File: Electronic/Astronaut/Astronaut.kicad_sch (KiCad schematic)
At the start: 67 parts, among them J1 Conn_01x05, J2 Conn_01x04, J3 Conn_01x02, J4 Conn_01x02, J5 Conn_01x04, J6 Conn_01x04, J7 Conn_01x02, J8 Conn_01x10, SW1 SH-1808SN-250GF, SW2 SH-1808SN-250GF, U1 LAN8651B1-E/LMX, U2 AVRH10C221KT1R5YA8, U3 AVRH10C221KT1R5YA8, U4 MCP2518FDT-E/SL, U5 ATA6563-GAQW1, U6 ESD5451N_C5261080, U7 ESD5451N_C5261080, U8 ADS1115IDGSR, X1 ABM10-25.000MHZ-D30-T3

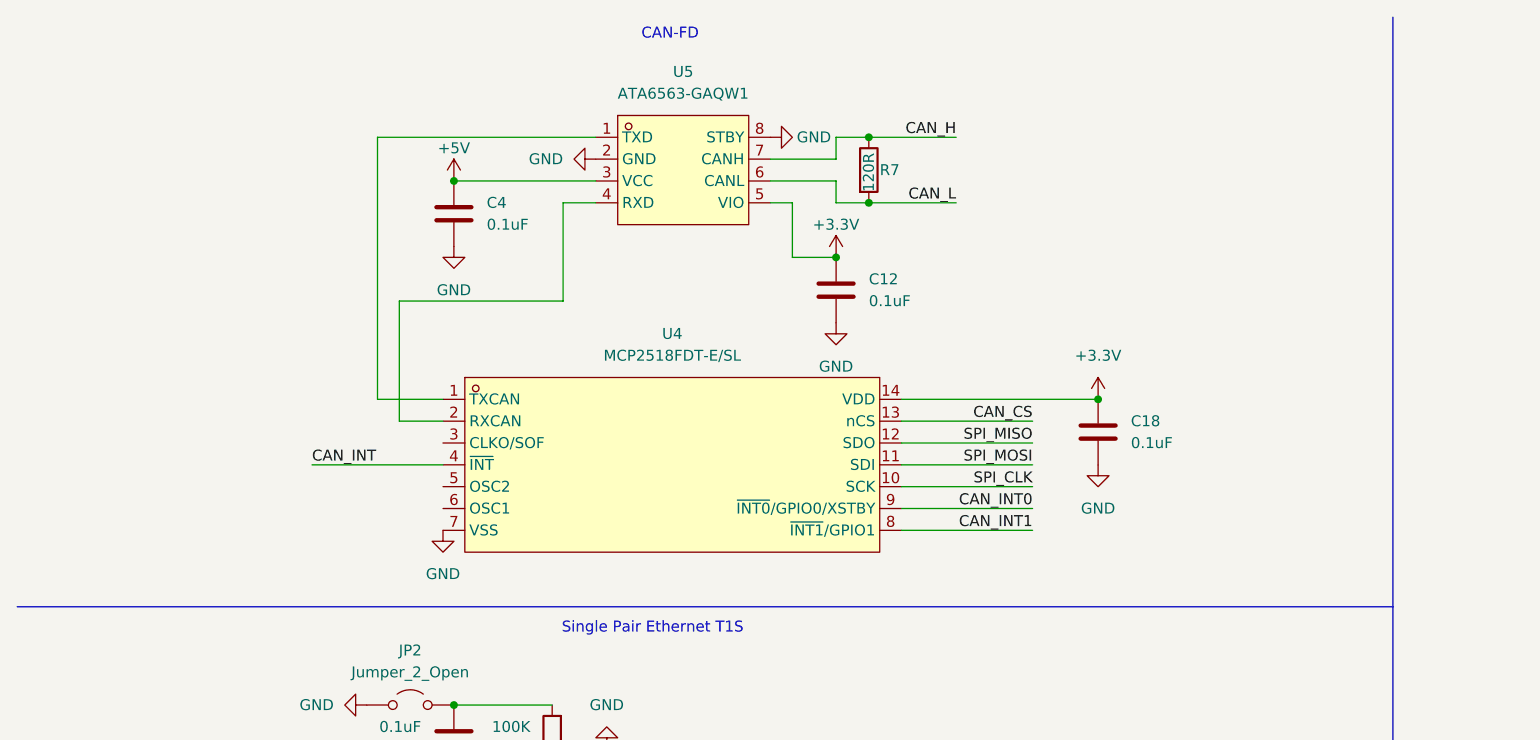
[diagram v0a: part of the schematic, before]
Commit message: Rename DisplayTTL to Astronaut
.. and removed can
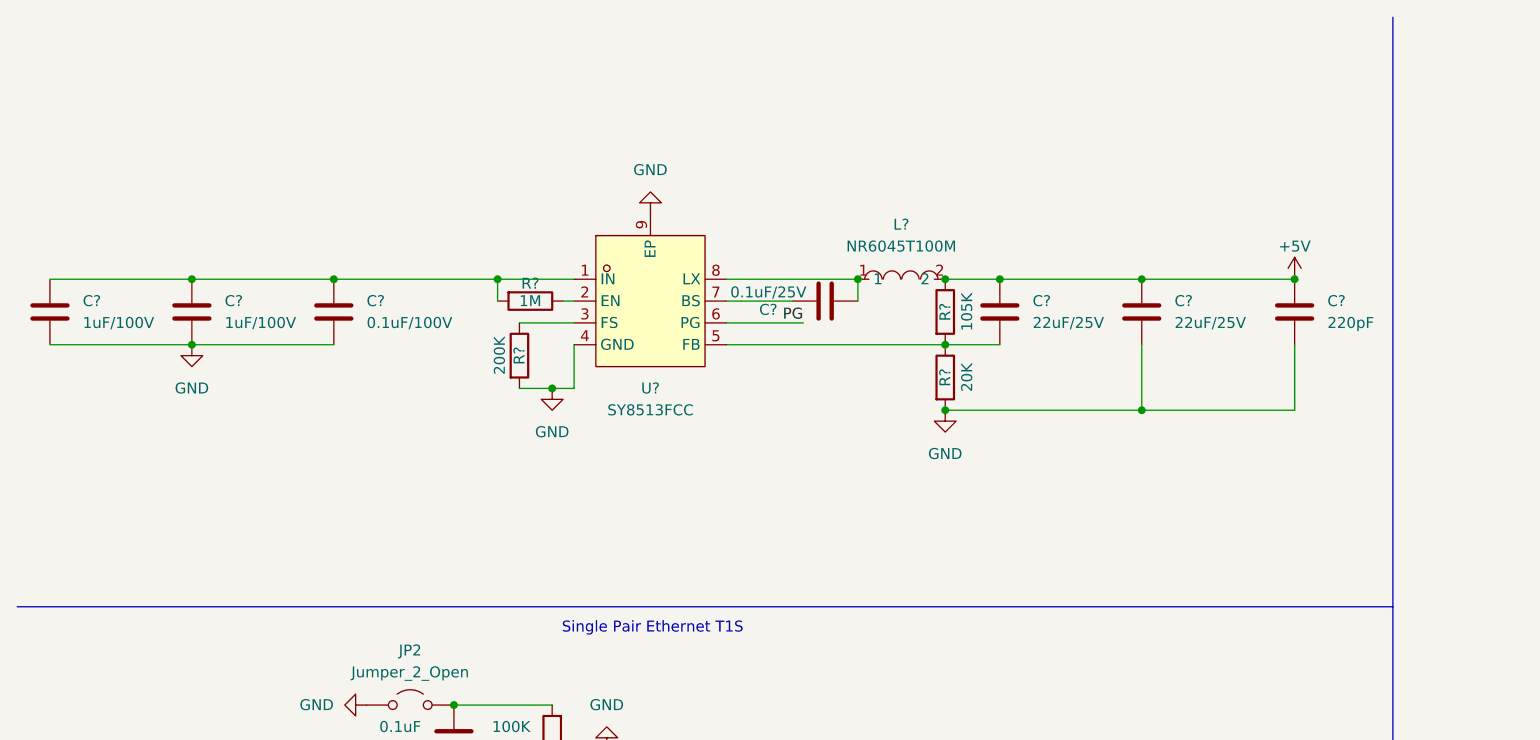
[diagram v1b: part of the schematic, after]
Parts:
- removed C12, C18, C4: 0.1uF, Capacitor_SMD:C_0402_1005Metric, symbol Device:C
- removed R7: 120R, symbol Device:R
- removed U4: MCP2518FDT-E/SL, lcsc:SOIC-14_L8.7-W3.9-P1.27-LS6.0-BL, symbol lcsc:MCP2518FDT-E_SL
- removed U5: ATA6563-GAQW1, lcsc:SOIC-8_L4.9-W3.9-P1.27-LS6.0-BL, symbol lcsc:ATA6563-GAQW1
- added C? (x2): 22uF/25V, symbol Device:C
- added C? (x2): 1uF/100V, symbol Device:C
- added C?: 0.1uF/25V, symbol Device:C
- added C?: 220pF, symbol Device:C
- added C?: 0.1uF/100V, symbol Device:C
- added L?: NR6045T100M, lcsc:IND-SMD_L6.0-W6.0_NR6045, symbol lcsc:NR6045T100M
- added R?: 200K, symbol Device:R
- added R?: 20K, symbol Device:R
- added R?: 1M, symbol Device:R
- added R?: 105K, symbol Device:R
- added U?: SY8513FCC, lcsc:SOP-8_L4.9-W3.9-P1.27-LS6.0-BL-EP3.1, symbol lcsc:SY8513FCC
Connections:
- net +5V: now also C?.1, C?.1, C?.1, L?.2, R?.1
- net GND: now also C?.2, C?.2, C?.2, C?.2, C?.2, R?.2, R?.2, U?.4 (GND), U?.9 (EP)
- new net: C?.2, L?.1, U?.8 (LX)
- new net: R?.1, U?.3 (FS)
- new net: C?.2, R?.1, R?.2, U?.5 (FB)
- new net: C?.1, C?.1, C?.1, R?.2, U?.1 (IN)
- new net: R?.1, U?.2 (EN)
- new net: C?.1, U?.7 (BS)
- new net PG: U?.6 (PG)
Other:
- note removed: "CAN-FD"

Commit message: WIP Astronaut : completed most of the routing / schematic : next audio / power protection
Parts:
- removed J1: Conn_01x05, Connector_PinSocket_2.54mm:PinSocket_1x05_P2.54mm_Vertical, symbol Connector:Conn_01x05_Socket
- removed J2, J5, J6: Conn_01x04, Connector_PinSocket_2.54mm:PinSocket_1x04_P2.54mm_Vertical, symbol Connector:Conn_01x04_Socket
- removed J4: Conn_01x02, Connector_PinSocket_2.54mm:PinSocket_1x02_P2.54mm_Vertical, symbol Connector:Conn_01x02_Socket
- removed J8: Conn_01x10, Connector_PinSocket_2.54mm:PinSocket_1x10_P2.54mm_Vertical, symbol Connector:Conn_01x10_Socket
- removed TP3, TP4: TestPoint, TestPoint:TestPoint_Pad_D1.5mm, symbol Connector:TestPoint
- added C27, C28: 10uF, Capacitor_SMD:C_0402_1005Metric, symbol Device:C
- added F1, F2: BSMD0805-110-6V, lcsc:F0805, symbol lcsc:BSMD0805-110-6V
- added J1: Conn_02x12_Counter_Clockwise, Connector_PinSocket_2.54mm:PinSocket_2x12_P2.54mm_Vertical, symbol Connector_Generic:Conn_02x12_Counter_Clockwise
- added U8: NCP1117ST33T3G, lcsc:SOT-223-3_L6.5-W3.4-P2.30-LS7.0-BR, symbol lcsc:NCP1117ST33T3G
- C1, C2, C3: renamed from C?; footprint (none) -> Capacitor_SMD:C_0805_2012Metric
- C14, C26: renamed from C?; footprint (none) -> Capacitor_SMD:C_0201_0603Metric
- C18, C21: renamed from C?; footprint (none) -> Capacitor_SMD:C_0402_1005Metric
- JP3: footprint (none) -> Jumper:SolderJumper-3_P1.3mm_Open_RoundedPad1.0x1.5mm_NumberLabels
- R10, R4, R5, R9: renamed from R?; footprint (none) -> Resistor_SMD:R_0201_0603Metric
- R11: renamed from R8; footprint (none) -> Resistor_SMD:R_0201_0603Metric
- R12: renamed from R9; footprint (none) -> Resistor_SMD:R_0201_0603Metric
- R13: renamed from R10; footprint (none) -> Resistor_SMD:R_0201_0603Metric
- R14: renamed from R11; footprint (none) -> Resistor_SMD:R_0201_0603Metric
- gave numbers to parts that had none: 2
- renumbered C8 to C10, C9 to C11, C10 to C12, C11 to C13, C13 to C15, C14 to C16, C15 to C17, C16 to C19, C17 to C20, C19 to C22, C20 to C23, C21 to C24, C22 to C25, C23 to C29, C24 to C30, C1 to C4, C2 to C5, C3 to C6, C5 to C7, C6 to C8, C7 to C9, J3 to J2, J7 to J3, L2 to L3, R4 to R6, R5 to R7, R6 to R8, U6 to U5, U7 to U6, U8 to U7
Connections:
- net +3V3 is gone; now on net +3.3V: C10.1, C13.1, C17.1, C20.1, C23.1, C25.1, L3.1, R8.2, U1.17 (VDDP), U1.4 (TEST), U1.7 (VDDP)
- net ADC4 is gone; now on net ADC2: U7.6 (AIN2)
- net +12V: now also C1.1, C2.1, C3.1, R5.2, U4.1 (IN)
- net +3.3V: now also C28.1, F2.2, U8.2 (OUTPUT), U8.4 (TAB)
- net +5V: now also C27.1, F1.2, U8.3 (INPUT)
- net ADC1: now also J1.23 (Pin_23)
- net ADC2: now also J1.21 (Pin_21)
- net GND: now also C27.2, C28.2, J1.12 (Pin_12), J1.19 (Pin_19), U8.1 (ADJ/GND)
- net GPIO_01: now also J1.6 (Pin_6)
- net GPIO_02: now also J1.5 (Pin_5)
- net GPIO_03: now also J1.1 (Pin_1)
- net GPIO_04: now also J1.2 (Pin_2)
- net GPIO_05: now also J1.4 (Pin_4)
- net GPIO_06: now also J1.3 (Pin_3)
- net I2C_SCL: now also J1.14 (Pin_14)
- net I2C_SDA: now also J1.13 (Pin_13)
- net SPI_CLK: now also J1.17 (Pin_17)
- net SPI_MISO: now also J1.20 (Pin_20)
- net SPI_MOSI: now also J1.18 (Pin_18)
- net TRX_N: no longer J2.2 (Pin_2)
- net TRX_P: no longer J2.1 (Pin_1)
- net UART1_RX: now also J1.9 (Pin_9)
- net UART1_TX: now also J1.11 (Pin_11)
- net UART2_RX: now also J1.16 (Pin_16)
- net UART2_TX: now also J1.15 (Pin_15)
- net USB_USER_D_N: now also J1.10 (Pin_10)
- net USB_USER_D_P: now also J1.8 (Pin_8)
- net at C5.1, R2.1, U2.2: now also J2.2 (Pin_2)
- net at C4.1, R3.1, U3.1: now also J2.1 (Pin_1)
- new net: F2.1, J1.22 (Pin_22)
- new net: F1.1, J1.24 (Pin_24)
- new net GPIO_07: J1.7 (Pin_7)
- no-connect marks 5 -> 7
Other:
- sheet Core1106 ports: added none; removed ADC0, ADC1
- sheet ESP32-P4 + C6 ports: added GPIO20, GPIO21; removed ADC1_CHANEL4, ADC1_CHANEL5, C6_IO6
- note added: "TODO : - ESD / surge protection"
- note removed: "TODO : - Current limiter - ESD / surge protection - Power supply"
- moved on the sheet: J2
